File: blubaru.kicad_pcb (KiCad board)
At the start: 2 copper layers, 80 x 79.5 mm, 68 parts, among them IC1 ATTINY4313-P, J1 DB15, J2 DB15, J3 TS5A22364-Q1, J4 TS5A22364-Q1, J5 RN52_BREAKOUT, J6 JACK_TRS_5PINS, J7 DRV632, J8 JACK_TRS_5PINS, P1 CONN_01X06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

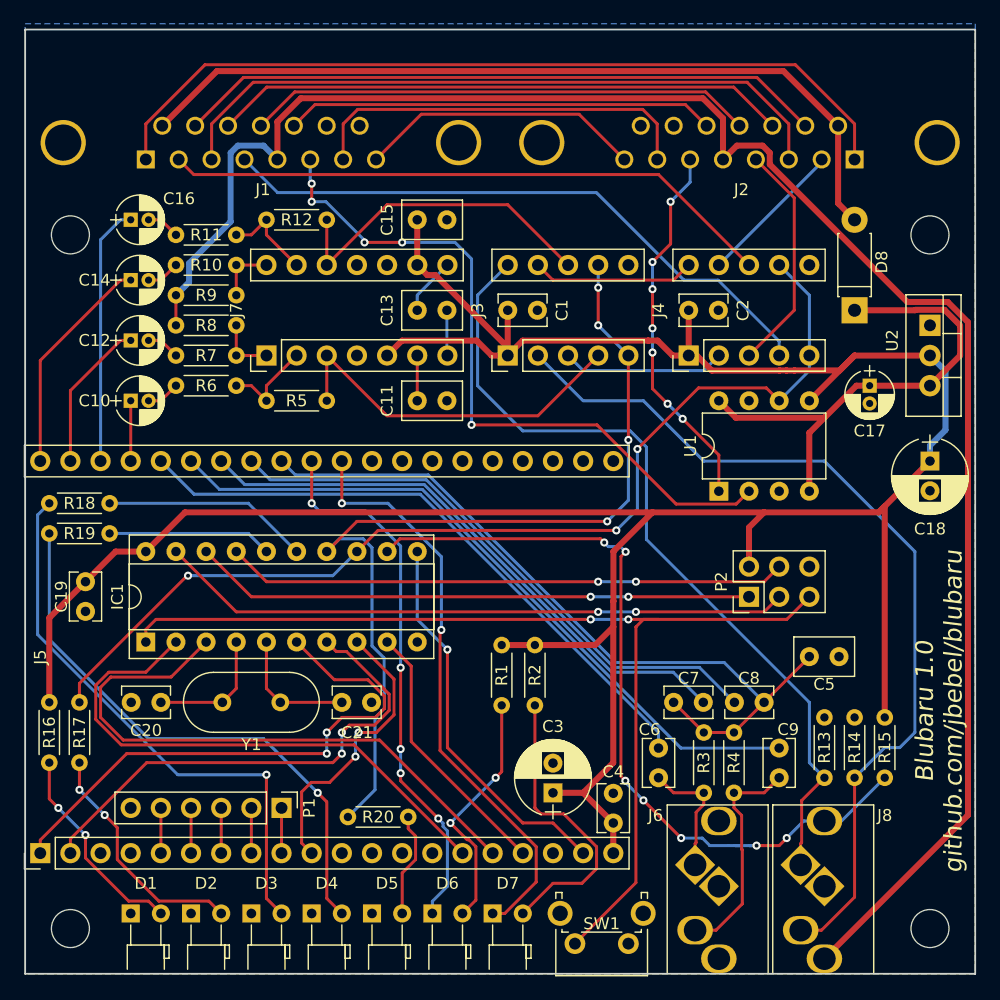
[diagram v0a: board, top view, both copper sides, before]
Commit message: Adjust some tolerances around traces and vias.
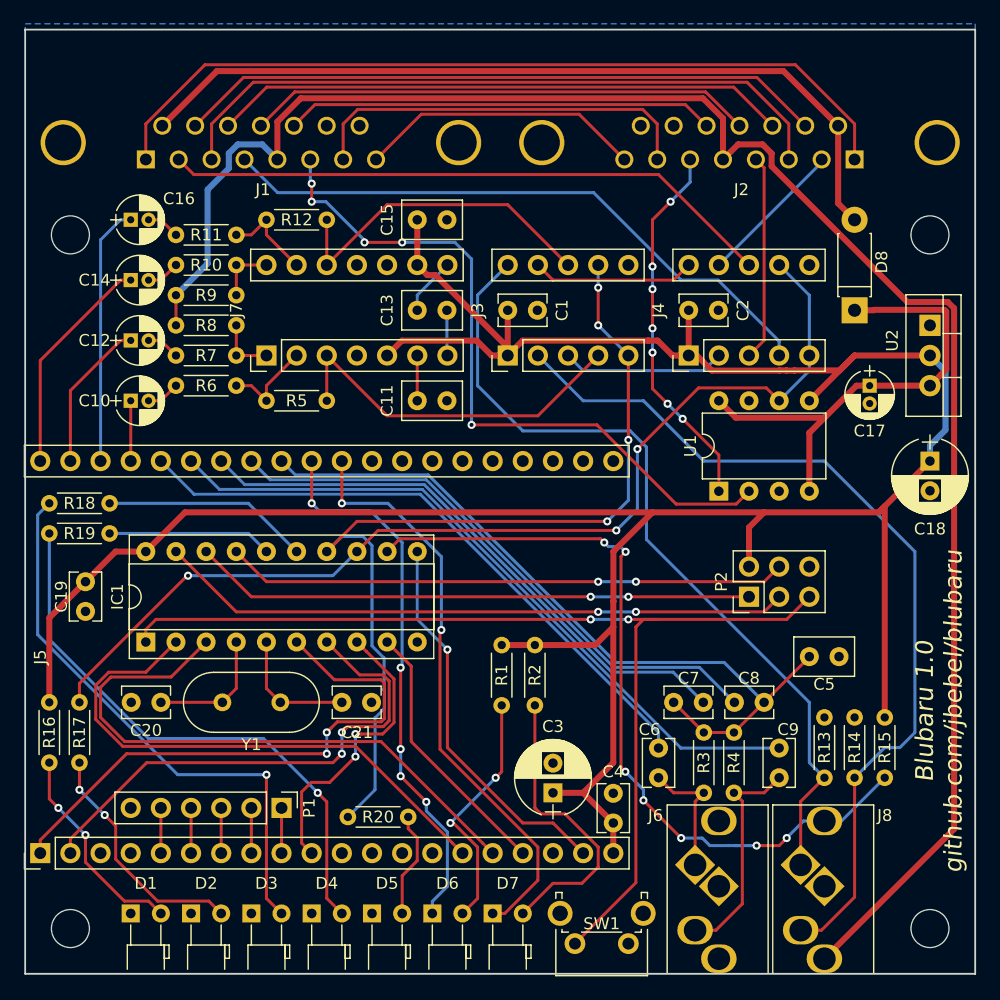
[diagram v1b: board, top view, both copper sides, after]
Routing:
- net /DB-15 interconnects/4_OUT: track 19.4 -> 17.3 mm
- net /DB-15 interconnects/Modules/Bluetooth Module/EVENT: track 42.0 -> 43.2 mm
- net /DB-15 interconnects/Modules/Microcontroller/BT_RESET: track 46.0 -> 47.2 mm
- net +12V: track 41.8 -> 40.8 mm
- net GNDA: track 153.3 -> 152.6 mm

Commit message: More layout tweaks for tolerances and appearance.
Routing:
- net /DB-15 interconnects/Modules/Audio switch/LINE_L: track 76.2 -> 65.9 mm
- net Net-(D3-Pad2): track 47.8 -> 51.8 mm
- net Net-(D4-Pad2): track 47.9 -> 51.7 mm
- net /DB-15 interconnects/4_IN: track 52.6 -> 54.9 mm
- net /DB-15 interconnects/2_OUT: track 12.5 -> 14.0 mm
- net /DB-15 interconnects/Modules/Line In/JACK_SENSE: track 68.3 -> 67.1 mm
- net GNDA: track 152.6 -> 153.3 mm
- net /DB-15 interconnects/Modules/Bluetooth Module/EVENT: track 43.2 -> 43.8 mm
- net /DB-15 interconnects/Modules/Bluetooth Module/UART_TX: track 46.7 -> 47.2 mm
- net /DB-15 interconnects/Modules/Bluetooth Module/PWR_EN: track 32.7 -> 33.2 mm
- net /DB-15 interconnects/Modules/Bluetooth Module/UART_RX: track 50.8 -> 51.3 mm
